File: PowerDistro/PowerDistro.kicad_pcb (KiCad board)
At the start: 2 copper layers, 70 x 70 mm, 10 parts

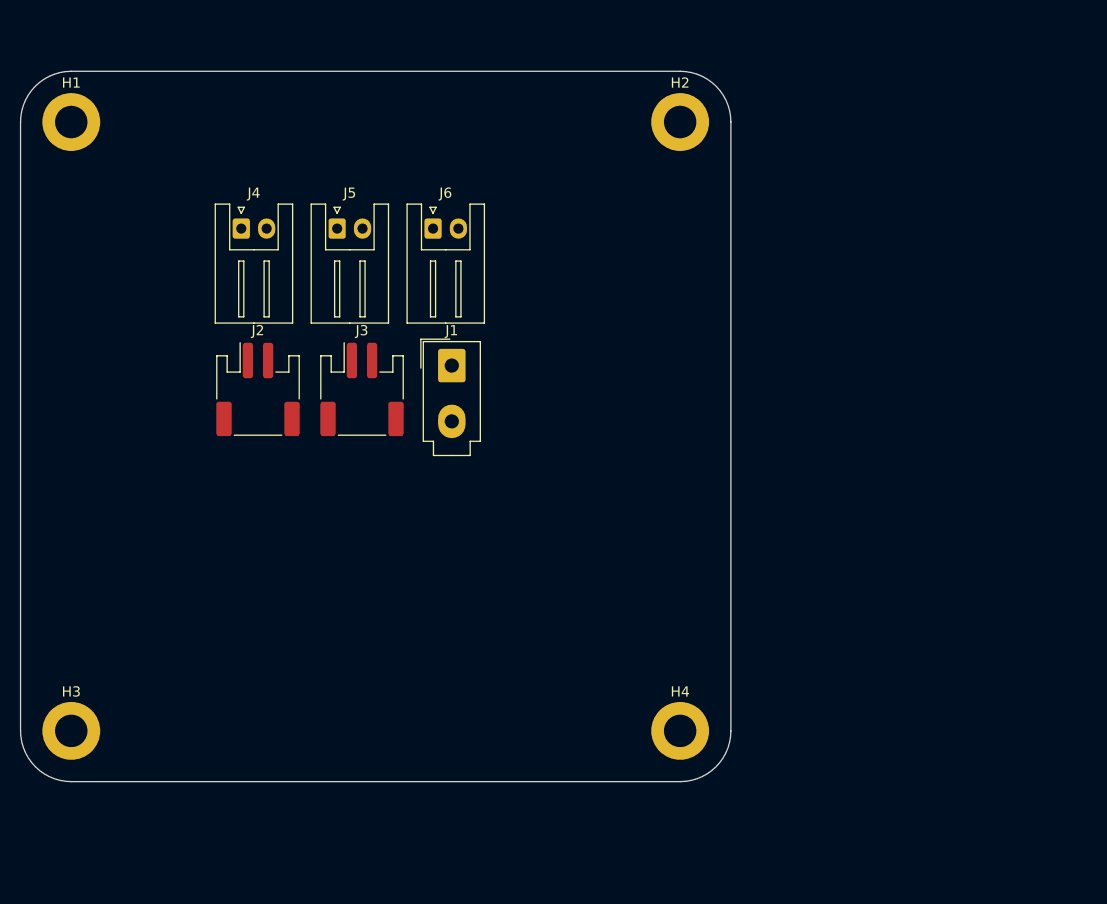
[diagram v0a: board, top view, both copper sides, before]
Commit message: Finished initial layout
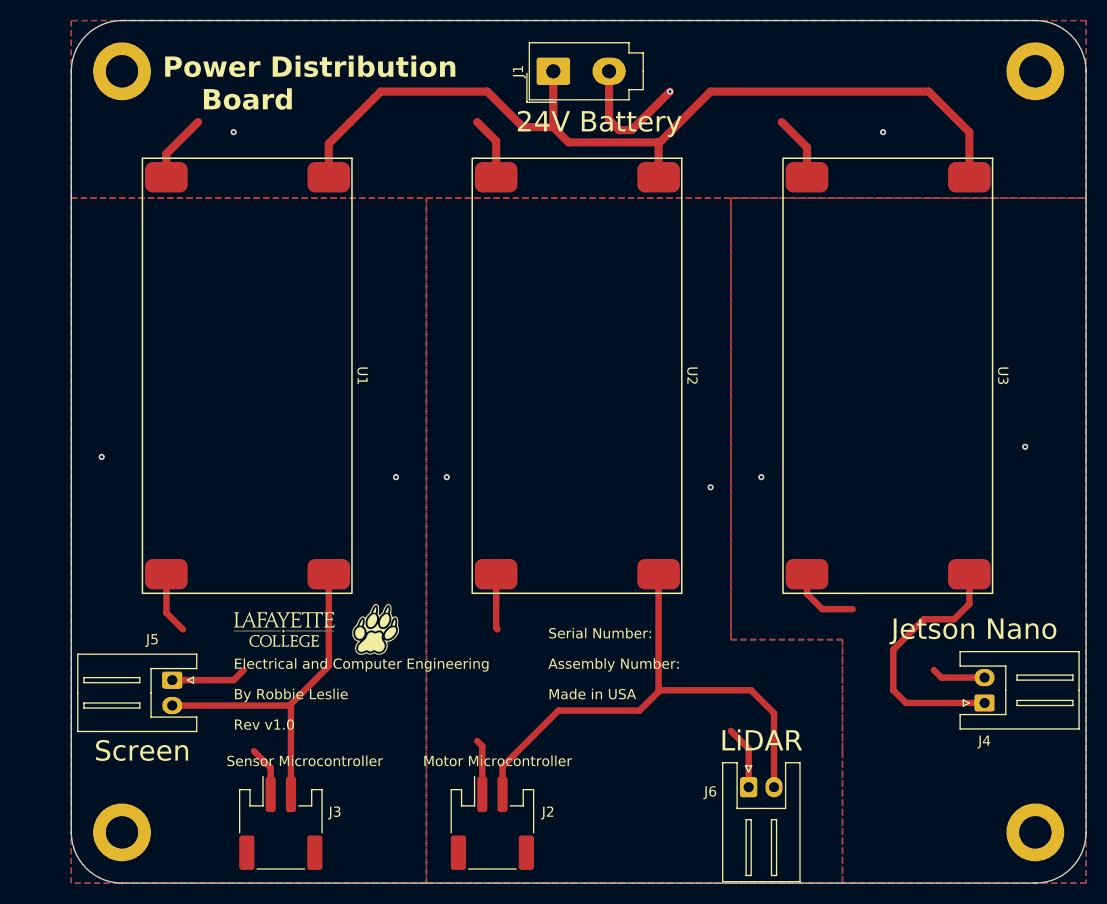
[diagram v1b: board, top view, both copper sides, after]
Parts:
- added G***: LOGO, Footprints:LeopardPawFootprint, F.Cu at (150.0, 105.0)
- added G***: LOGO, LOGO, F.Cu at (141.0, 105.0)
- added U1: ~, Regulator_Boards:LM2596, F.Cu at (137.5, 80.0)
- added U2: ~, Regulator_Boards:LM2596, F.Cu at (170.0, 80.0)
- added U3: ~, Regulator_Boards:LM2596, F.Cu at (200.6, 80.0)
- moved J4 86.9 mm to (210.0, 112.2), turned to 90 degrees
- moved J6 63.2 mm to (186.8, 120.5)
- moved J2 48.6 mm to (161.5, 124.1)
- moved J5 47.4 mm to (129.9, 110.0), turned to -90 degrees
- moved J3 43.5 mm to (140.7, 124.1)
- moved H4 36.4 mm to (215.0, 125.0)
- moved H2 35.4 mm to (215.0, 50.0)
- moved J1 30.7 mm to (167.5, 50.0), turned to 90 degrees
- moved H3 11.2 mm to (125.0, 125.0)
- moved H1 7.07 mm to (125.0, 50.0)
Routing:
- net +BATT: track 0.00 -> 87.7 mm
- net /12V Reg2: track 0.00 -> 53.3 mm
- net /12V Reg1: track 0.00 -> 35.8 mm
- net -BATT: track 0.00 -> 32.2 mm, vias 0 -> 3
- net /19V: track 0.00 -> 25.8 mm
- net /Reg1 GND: track 0.00 -> 19.4 mm, vias 0 -> 2
- net /Reg2 GND: track 0.00 -> 18.1 mm, vias 0 -> 2
- net /19V GND: track 0.00 -> 12.4 mm, vias 0 -> 2
- added copper zone on B.Cu, net -BATT
- added copper zone on F.Cu, net -BATT
- added copper zone on B.Cu, net /19V GND
- added copper zone on F.Cu, net /19V GND
- added copper zone on B.Cu, net /Reg1 GND
- added copper zone on F.Cu, net /Reg1 GND
- added copper zone on B.Cu, net /Reg2 GND
- added copper zone on F.Cu, net /Reg2 GND
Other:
- board size 70 x 70 mm -> 100 x 85 mm
- board text added: "Assembly Number:"
- board text added: "Board Part Number:"
- board text added: "By Robbie Leslie"
- board text added: "Electrical and Computer Engineering"
- board text added: "Made in USA"
- board text added: "Power Distribution Board"
- board text added: "Rev v1.0"
- board text added: "Serial Number:"

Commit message: Updated PCB Layout
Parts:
- added Q1: DMT6009LCT, Package_TO_SOT_THT:TO-220-3_Vertical, F.Cu at (176.2, 124.5)
- added R1: 174, Resistor_SMD:R_0805_2012Metric, F.Cu at (147.7, 115.1)
- added U4: Optoisolators, Package_SO:SO-5-6_4.55x3.7mm_P1.27mm, F.Cu at (161.8, 112.5)
- J3: value ~ -> 12V; footprint Connector_JST:JST_PH_S2B-PH-SM4-TB_1x02-1MP_P2.00mm_Horizontal -> Connector_JST:JST_PH_S3B-PH-SM4-TB_1x03-1MP_P2.00mm_Horizontal
- moved J3 0.26 mm to (140.7, 123.8)
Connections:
- J6 pad 1: /Reg2 GND -> /LiDAR GND
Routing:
- net /LiDAR Wire: track 0.00 -> 20.8 mm
- net /LiDAR GND: track 0.00 -> 20.5 mm
- net /12V Reg2: track 53.3 -> 68.4 mm, vias 0 -> 2
- net Net-(U4-Anode): track 0.00 -> 11.6 mm
- net /LiDAR On Pin: track 0.00 -> 9.23 mm
- net /Reg2 GND: track 18.1 -> 10.6 mm
- net /Reg1 GND: track 19.4 -> 23.5 mm
- net /12V Reg1: track 35.8 -> 34.9 mm
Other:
- board text added: "12V"
- board text added: "19V"
